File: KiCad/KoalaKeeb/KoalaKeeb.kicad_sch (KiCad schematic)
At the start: 31 parts, among them J1 JLC_Battery_Con_L, SW1 Switch_SW_Push, SW10 Switch_SW_Push, SW11 Switch_SW_Push, SW12 Switch_SW_Push, SW13 Switch_SW_Push, SW14 Switch_SW_Push, SW15 Switch_SW_Push, SW19 Switch_SW_Push, SW2 Switch_SW_Push, SW20 Switch_SW_Push, SW3 Switch_SW_Push, SW4 Switch_SW_Push, SW5 Switch_SW_Push, SW6 Switch_SW_Push, SW7 Switch_SW_Push, SW8 Switch_SW_Push, SW9 Switch_SW_Push, U1 Nice!Nano_L

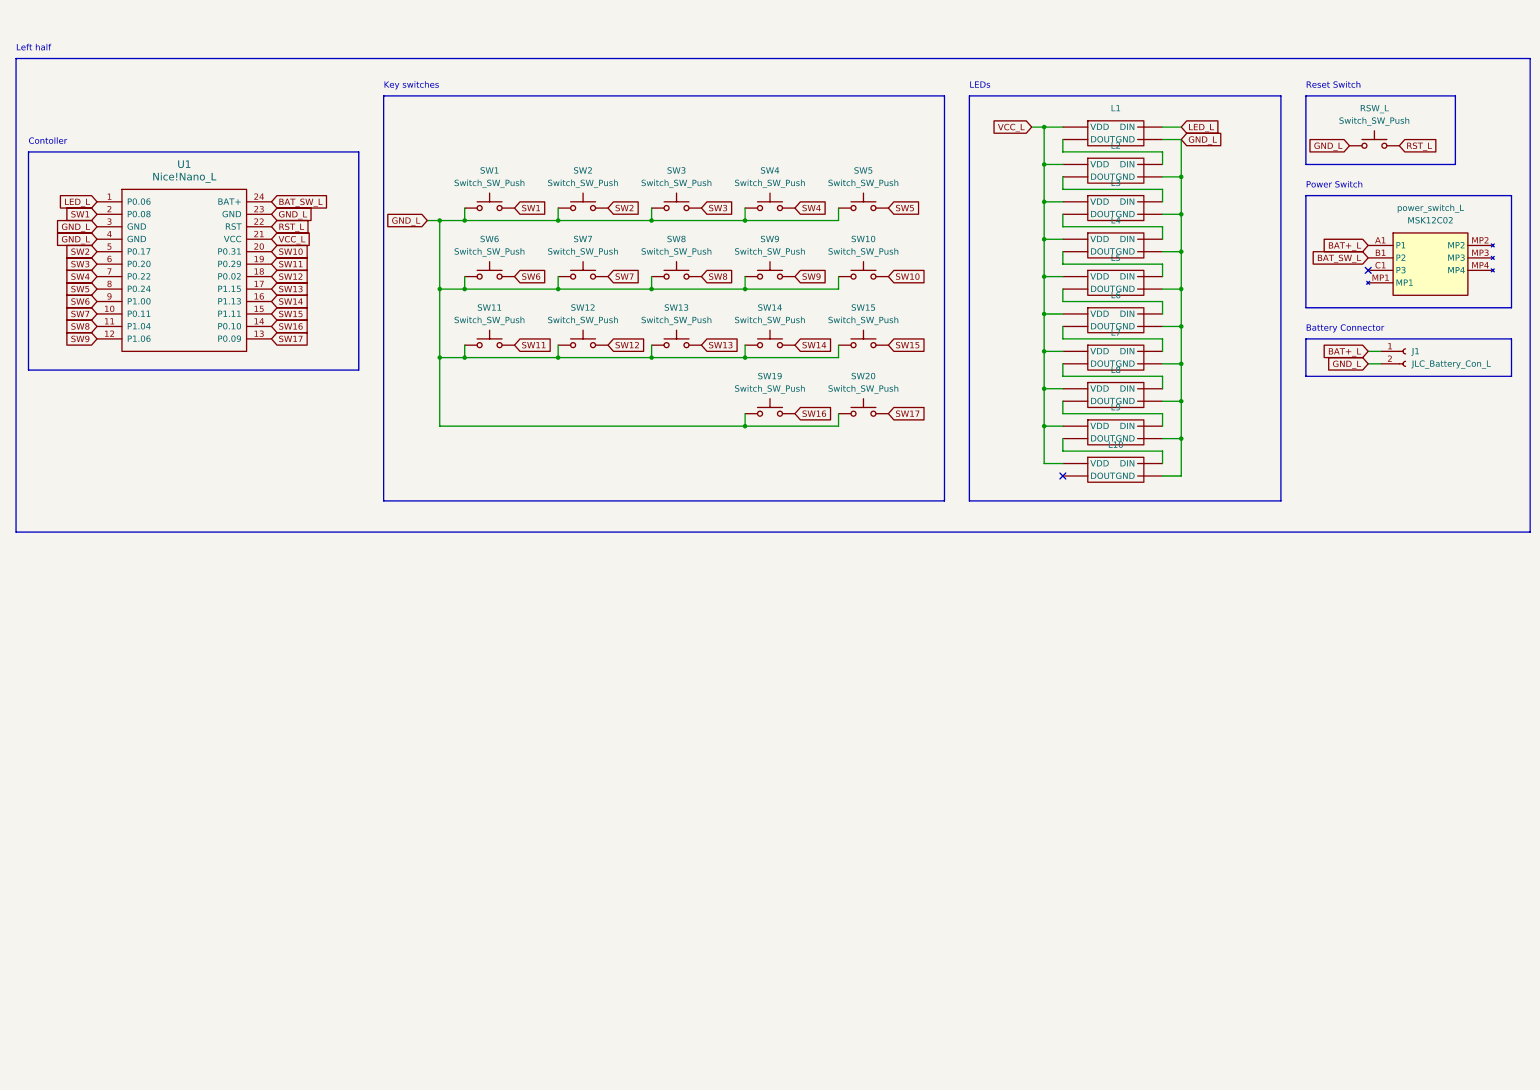
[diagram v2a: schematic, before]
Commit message: add right half
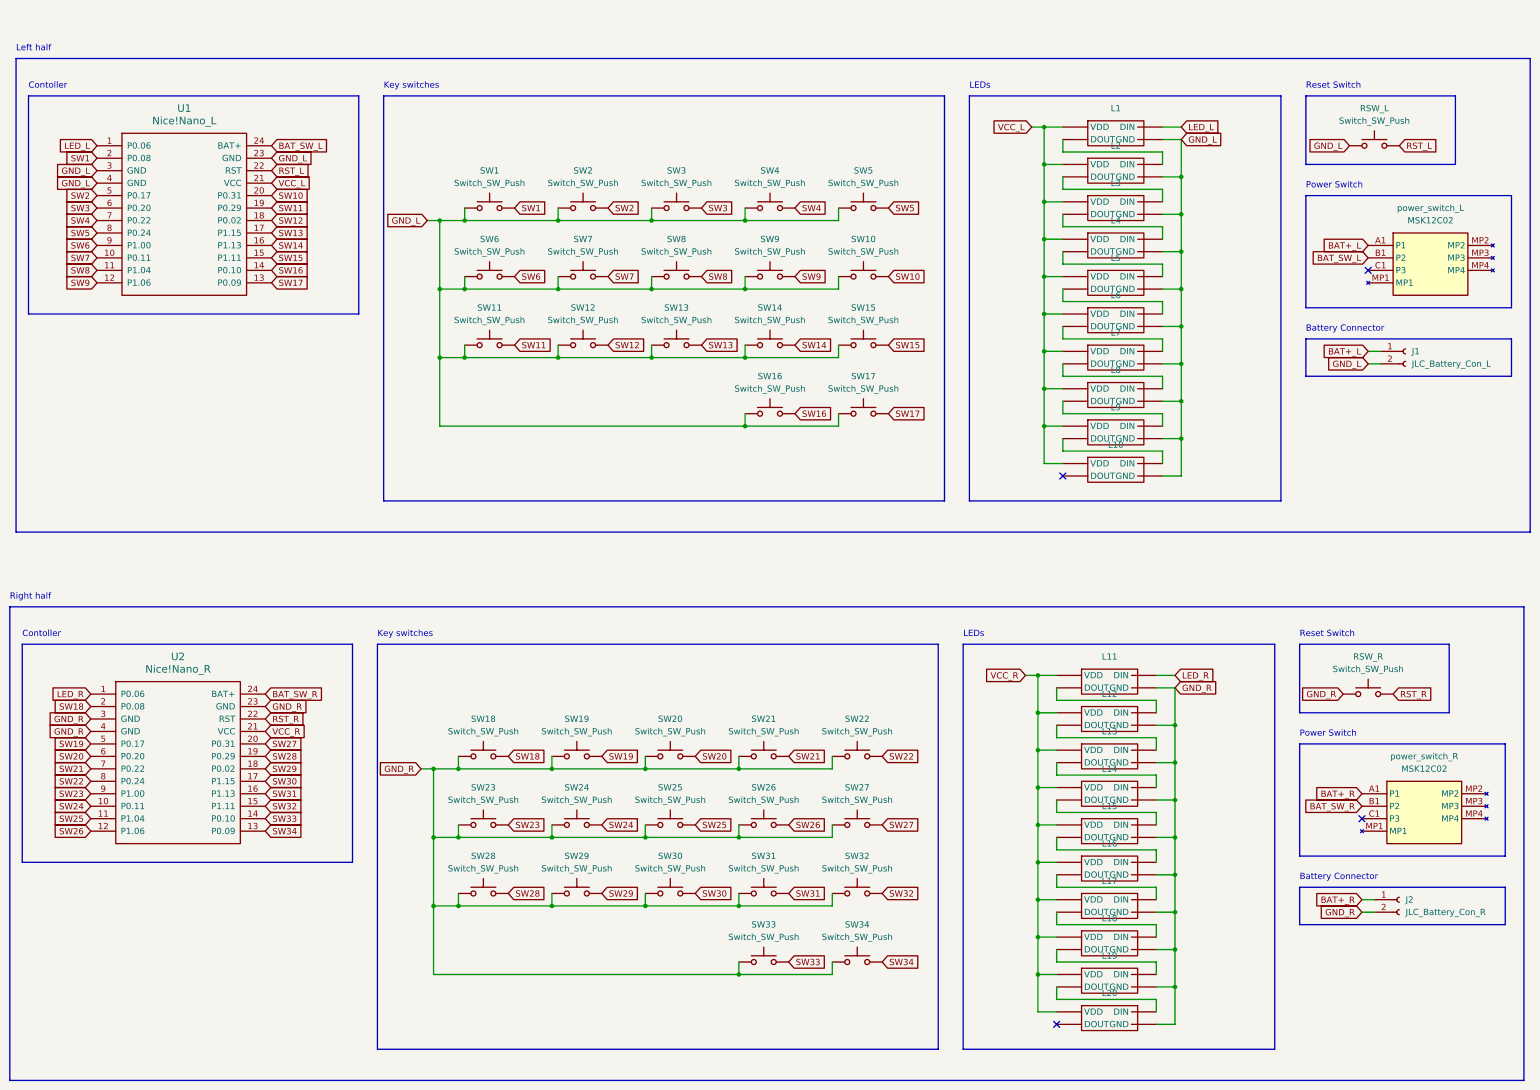
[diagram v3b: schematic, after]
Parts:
- added J2: JLC_Battery_Con_R, symbol Connector:Conn_01x02_Socket
- added L11, L12, L13, L14, L15, L16, L17, L18, L19, L20: ~, symbol KoalaKeeb-cache:SK6812_MINI-E
- added RSW_R, SW18, SW19, SW20, SW21, SW22, SW23, SW24, SW25, SW26, SW27, SW28, SW29, SW30, SW31, SW32, SW33, SW34: Switch_SW_Push, symbol KoalaKeeb-cache:Switch_SW_Push
- added U2: Nice!Nano_R, symbol KoalaKeeb-cache:Nice!Nano
- added power_switch_R: MSK12C02, MSK12C02, symbol KoalaKeeb-cache:MSK12C02
- renumbered SW19 to SW16, SW20 to SW17
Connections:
- new net: L18. (VDD), L19. (VDD)
- new net: L17. (VDD), L18. (VDD)
- new net: L12. (VDD), L13. (VDD)
- new net: L11. (VDD), L12. (VDD)
- new net: L10. (VDD), L9. (VDD)
- new net: L19. (VDD), L20. (VDD)
- new net: L6. (VDD), L7. (VDD)
- new net: L7. (VDD), L8. (VDD)
- new net: L13. (VDD), L14. (VDD)
- new net: L14. (VDD), L15. (VDD)
- new net: L4. (VDD), L5. (VDD)
- new net: L3. (VDD), L4. (VDD)
- new net: L15. (VDD), L16. (VDD)
- new net: L16. (VDD), L17. (VDD)
- new net: L1. (VDD), L2. (VDD)
- new net: L5. (VDD), L6. (VDD)
- new net: L2. (VDD), L3. (VDD)
- new net: L8. (VDD), L9. (VDD)
- new net BAT+_R: J2.1 (Pin_1), power_switch_R.A1 (P1)
- new net BAT_SW_R: U2.24 (BAT+), power_switch_R.B1 (P2)
- new net GND_R: J2.2 (Pin_2), L11. (VDD), L12. (VDD), L13. (VDD), L14. (VDD), L15. (VDD), L16. (VDD), L17. (VDD), L18. (VDD), L19. (VDD), L20. (VDD), RSW_R.1, SW18.1, SW19.1, SW20.1, SW21.1, SW22.1, SW23.1, SW24.1, SW25.1, SW26.1, SW27.1, SW28.1, SW29.1, SW30.1, SW31.1, SW32.1, SW33.1, SW34.1, U2.23 (GND), U2.3 (GND), U2.4 (GND)
- new net LED_R: L11. (VDD), U2.1 (P0.06)
- new net RST_R: RSW_R.2, U2.22 (RST)
- new net SW18: SW18.2, U2.2 (P0.08)
- new net SW19: SW19.2, U2.5 (P0.17)
- new net SW20: SW20.2, U2.6 (P0.20)
- new net SW21: SW21.2, U2.7 (P0.22)
- new net SW22: SW22.2, U2.8 (P0.24)
- new net SW23: SW23.2, U2.9 (P1.00)
- new net SW24: SW24.2, U2.10 (P0.11)
- new net SW25: SW25.2, U2.11 (P1.04)
- new net SW26: SW26.2, U2.12 (P1.06)
- new net SW27: SW27.2, U2.20 (P0.31)
- new net SW28: SW28.2, U2.19 (P0.29)
- new net SW29: SW29.2, U2.18 (P0.02)
- new net SW30: SW30.2, U2.17 (P1.15)
- new net SW31: SW31.2, U2.16 (P1.13)
- new net SW32: SW32.2, U2.15 (P1.11)
- new net SW33: SW33.2, U2.14 (P0.10)
- new net SW34: SW34.2, U2.13 (P0.09)
- new net VCC_R: L11. (VDD), L12. (VDD), L13. (VDD), L14. (VDD), L15. (VDD), L16. (VDD), L17. (VDD), L18. (VDD), L19. (VDD), L20. (VDD), U2.21 (VCC)
- no-connect marks 2 -> 4
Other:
- note added: "Right half"
- moved on the sheet: U1

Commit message: add and assing most footprints
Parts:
- L1, L10, L11, L12, L13, L14, L15, L16, L17, L18, L19, L2, L20, L3, L4, L5, L6, L7, L8, L9: footprint (none) -> KoalaKeeb:SK6812-MINI-E
- SW1, SW10, SW11, SW12, SW13, SW14, SW15, SW16, SW17, SW18, SW19, SW2, SW20, SW21, SW22, SW23, SW24, SW25, SW26, SW27, SW28, SW29, SW3, SW30, SW31, SW32, SW33, SW34, SW4, SW5, SW6, SW7, SW8, SW9: footprint (none) -> KoalaKeeb:Kailh_socket_PG1350
- U1, U2: footprint (none) -> KoalaKeeb:nice!nano
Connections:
- new net: L18. (VDD), L19. (VDD)
- new net: L17. (VDD), L18. (VDD)
- new net: L12. (VDD), L13. (VDD)
- new net: L11. (VDD), L12. (VDD)
- new net: L10. (VDD), L9. (VDD)
- new net: L19. (VDD), L20. (VDD)
- new net: L6. (VDD), L7. (VDD)
- new net: L7. (VDD), L8. (VDD)
- new net: L13. (VDD), L14. (VDD)
- new net: L14. (VDD), L15. (VDD)
- new net: L4. (VDD), L5. (VDD)
- new net: L3. (VDD), L4. (VDD)
- new net: L15. (VDD), L16. (VDD)
- new net: L16. (VDD), L17. (VDD)
- new net: L1. (VDD), L2. (VDD)
- new net: L5. (VDD), L6. (VDD)
- new net: L2. (VDD), L3. (VDD)
- new net: L8. (VDD), L9. (VDD)

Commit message: add remaining footprints and create PCB
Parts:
- J1, J2: footprint (none) -> KoalaKeeb:JLC 2Pin
- RSW_L1: renamed from RSW_L; footprint (none) -> KoalaKeeb:TS-1136-4.3
- RSW_R1: renamed from RSW_R; footprint (none) -> KoalaKeeb:TS-1136-4.3
- power_switch_L1: renamed from power_switch_L; footprint MSK12C02 -> KoalaKeeb:MSK12C02
- power_switch_R1: renamed from power_switch_R; footprint MSK12C02 -> KoalaKeeb:MSK12C02
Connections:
- net GND_L: now also L1.3 (GND), L10.3 (GND), L2.3 (GND), L3.3 (GND), L4.3 (GND), L5.3 (GND), L6.3 (GND), L7.3 (GND), L8.3 (GND), L9.3 (GND); no longer L1. (VDD), L10. (VDD), L2. (VDD), L3. (VDD), L4. (VDD), L5. (VDD), L6. (VDD), L7. (VDD), L8. (VDD), L9. (VDD)
- net GND_R: now also L11.3 (GND), L12.3 (GND), L13.3 (GND), L14.3 (GND), L15.3 (GND), L16.3 (GND), L17.3 (GND), L18.3 (GND), L19.3 (GND), L20.3 (GND); no longer L11. (VDD), L12. (VDD), L13. (VDD), L14. (VDD), L15. (VDD), L16. (VDD), L17. (VDD), L18. (VDD), L19. (VDD), L20. (VDD)
- net LED_L: now also L1.4 (DIN); no longer L1. (VDD)
- net LED_R: now also L11.4 (DIN); no longer L11. (VDD)
- net VCC_L: now also L1.1 (VDD), L10.1 (VDD), L2.1 (VDD), L3.1 (VDD), L4.1 (VDD), L5.1 (VDD), L6.1 (VDD), L7.1 (VDD), L8.1 (VDD), L9.1 (VDD); no longer L1. (VDD), L10. (VDD), L2. (VDD), L3. (VDD), L4. (VDD), L5. (VDD), L6. (VDD), L7. (VDD), L8. (VDD), L9. (VDD)
- net VCC_R: now also L11.1 (VDD), L12.1 (VDD), L13.1 (VDD), L14.1 (VDD), L15.1 (VDD), L16.1 (VDD), L17.1 (VDD), L18.1 (VDD), L19.1 (VDD), L20.1 (VDD); no longer L11. (VDD), L12. (VDD), L13. (VDD), L14. (VDD), L15. (VDD), L16. (VDD), L17. (VDD), L18. (VDD), L19. (VDD), L20. (VDD)
- new net: L18.2 (DOUT), L19.4 (DIN)
- new net: L17.2 (DOUT), L18.4 (DIN)
- new net: L12.2 (DOUT), L13.4 (DIN)
- new net: L11.2 (DOUT), L12.4 (DIN)
- new net: L10.4 (DIN), L9.2 (DOUT)
- new net: L19.2 (DOUT), L20.4 (DIN)
- new net: L7.2 (DOUT), L8.4 (DIN)
- new net: L6.2 (DOUT), L7.4 (DIN)
- new net: L14.2 (DOUT), L15.4 (DIN)
- new net: L13.2 (DOUT), L14.4 (DIN)
- new net: L4.2 (DOUT), L5.4 (DIN)
- new net: L3.2 (DOUT), L4.4 (DIN)
- new net: L15.2 (DOUT), L16.4 (DIN)
- new net: L16.2 (DOUT), L17.4 (DIN)
- new net: L1.2 (DOUT), L2.4 (DIN)
- new net: L5.2 (DOUT), L6.4 (DIN)
- new net: L2.2 (DOUT), L3.4 (DIN)
- new net: L8.2 (DOUT), L9.4 (DIN)
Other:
- moved on the sheet: SW33, SW34

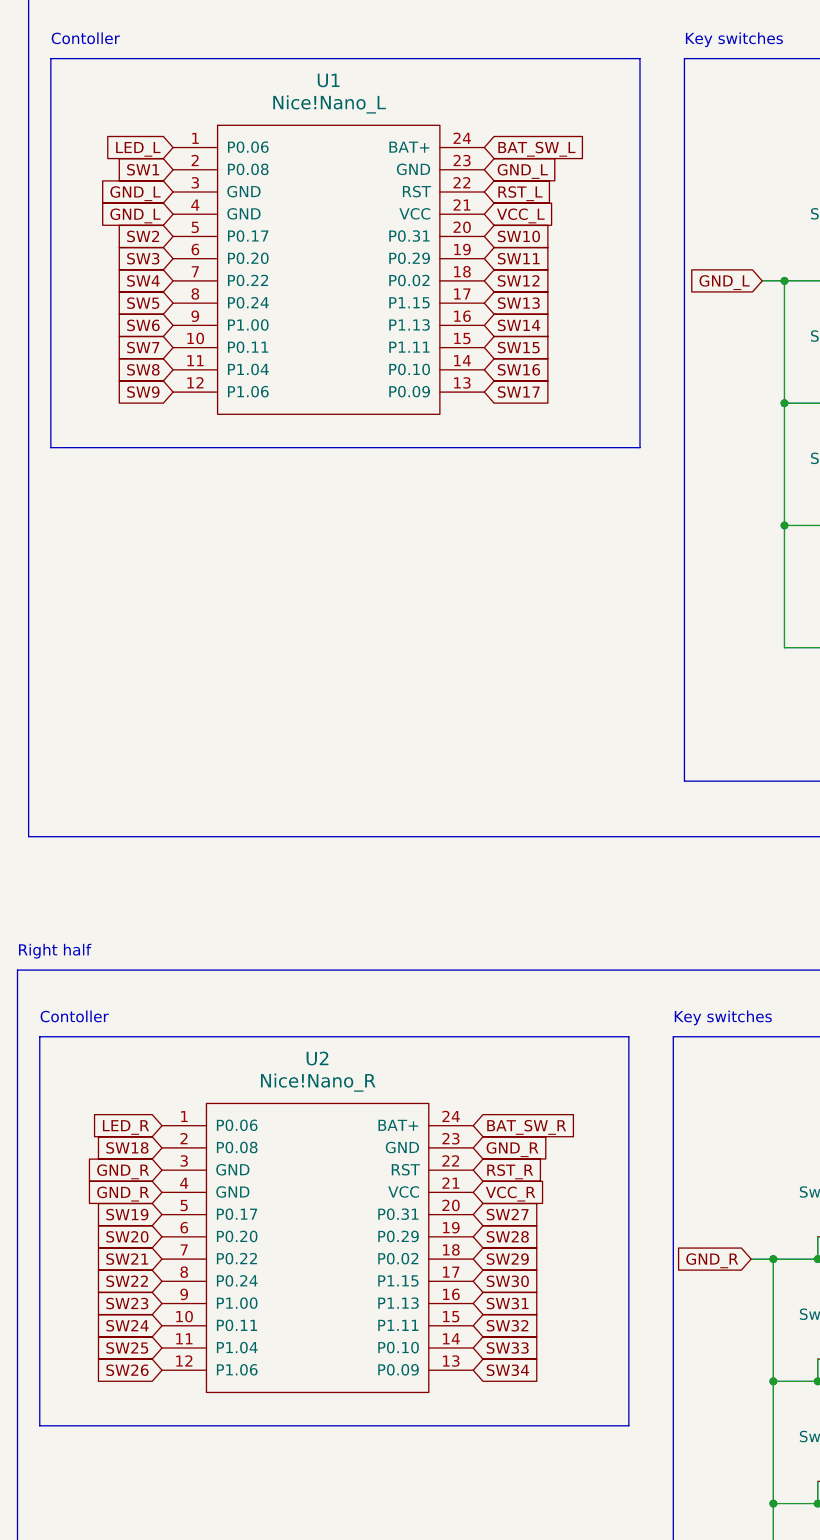
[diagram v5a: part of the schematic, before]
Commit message: routing and outlines done
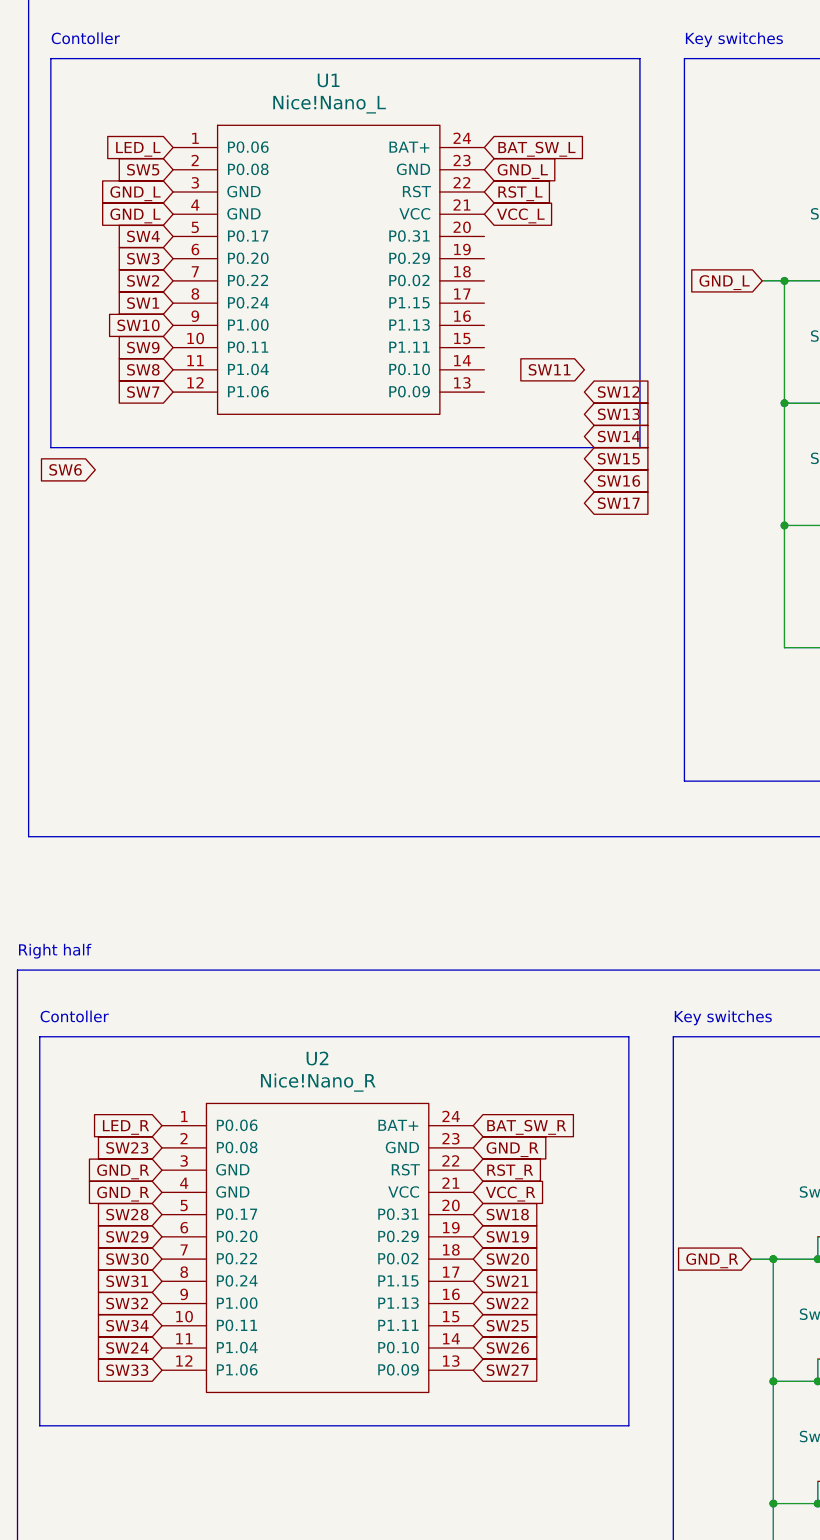
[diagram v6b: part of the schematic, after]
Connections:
- net SW1: now also U1.8 (P0.24); no longer U1.2 (P0.08)
- net SW10: now also U1.9 (P1.00); no longer U1.20 (P0.31)
- net SW11: no longer U1.19 (P0.29)
- net SW12: no longer U1.18 (P0.02)
- net SW13: no longer U1.17 (P1.15)
- net SW14: no longer U1.16 (P1.13)
- net SW15: no longer U1.15 (P1.11)
- net SW16: no longer U1.14 (P0.10)
- net SW17: no longer U1.13 (P0.09)
- net SW18: now also U2.20 (P0.31); no longer U2.2 (P0.08)
- net SW19: now also U2.19 (P0.29); no longer U2.5 (P0.17)
- net SW2: now also U1.7 (P0.22); no longer U1.5 (P0.17)
- net SW20: now also U2.18 (P0.02); no longer U2.6 (P0.20)
- net SW21: now also U2.17 (P1.15); no longer U2.7 (P0.22)
- net SW22: now also U2.16 (P1.13); no longer U2.8 (P0.24)
- net SW23: now also U2.2 (P0.08); no longer U2.9 (P1.00)
- net SW24: now also U2.11 (P1.04); no longer U2.10 (P0.11)
- net SW25: now also U2.15 (P1.11); no longer U2.11 (P1.04)
- net SW26: now also U2.14 (P0.10); no longer U2.12 (P1.06)
- net SW27: now also U2.13 (P0.09); no longer U2.20 (P0.31)
- net SW28: now also U2.5 (P0.17); no longer U2.19 (P0.29)
- net SW29: now also U2.6 (P0.20); no longer U2.18 (P0.02)
- net SW30: now also U2.7 (P0.22); no longer U2.17 (P1.15)
- net SW31: now also U2.8 (P0.24); no longer U2.16 (P1.13)
- net SW32: now also U2.9 (P1.00); no longer U2.15 (P1.11)
- net SW33: now also U2.12 (P1.06); no longer U2.14 (P0.10)
- net SW34: now also U2.10 (P0.11); no longer U2.13 (P0.09)
- net SW4: now also U1.5 (P0.17); no longer U1.7 (P0.22)
- net SW5: now also U1.2 (P0.08); no longer U1.8 (P0.24)
- net SW6: no longer U1.9 (P1.00)
- net SW7: now also U1.12 (P1.06); no longer U1.10 (P0.11)
- net SW9: now also U1.10 (P0.11); no longer U1.12 (P1.06)
